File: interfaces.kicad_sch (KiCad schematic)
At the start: 92 parts, among them IC3 TPD8S009DSMR, J6 685119134923, J7 693071020811, J9 USB4105-GF-A, Q1 BSS138APW, Q10 BSS138APW, Q2 BSS138APW, Q3 BSS138APW, Q4 BSS138APW, Q5 BSS138APW, Q6 BSS138APW, Q9 BSS138APW, U7 FT4232HQ, Y2 ABM8G-12.000MHZ-18-D2Y-T

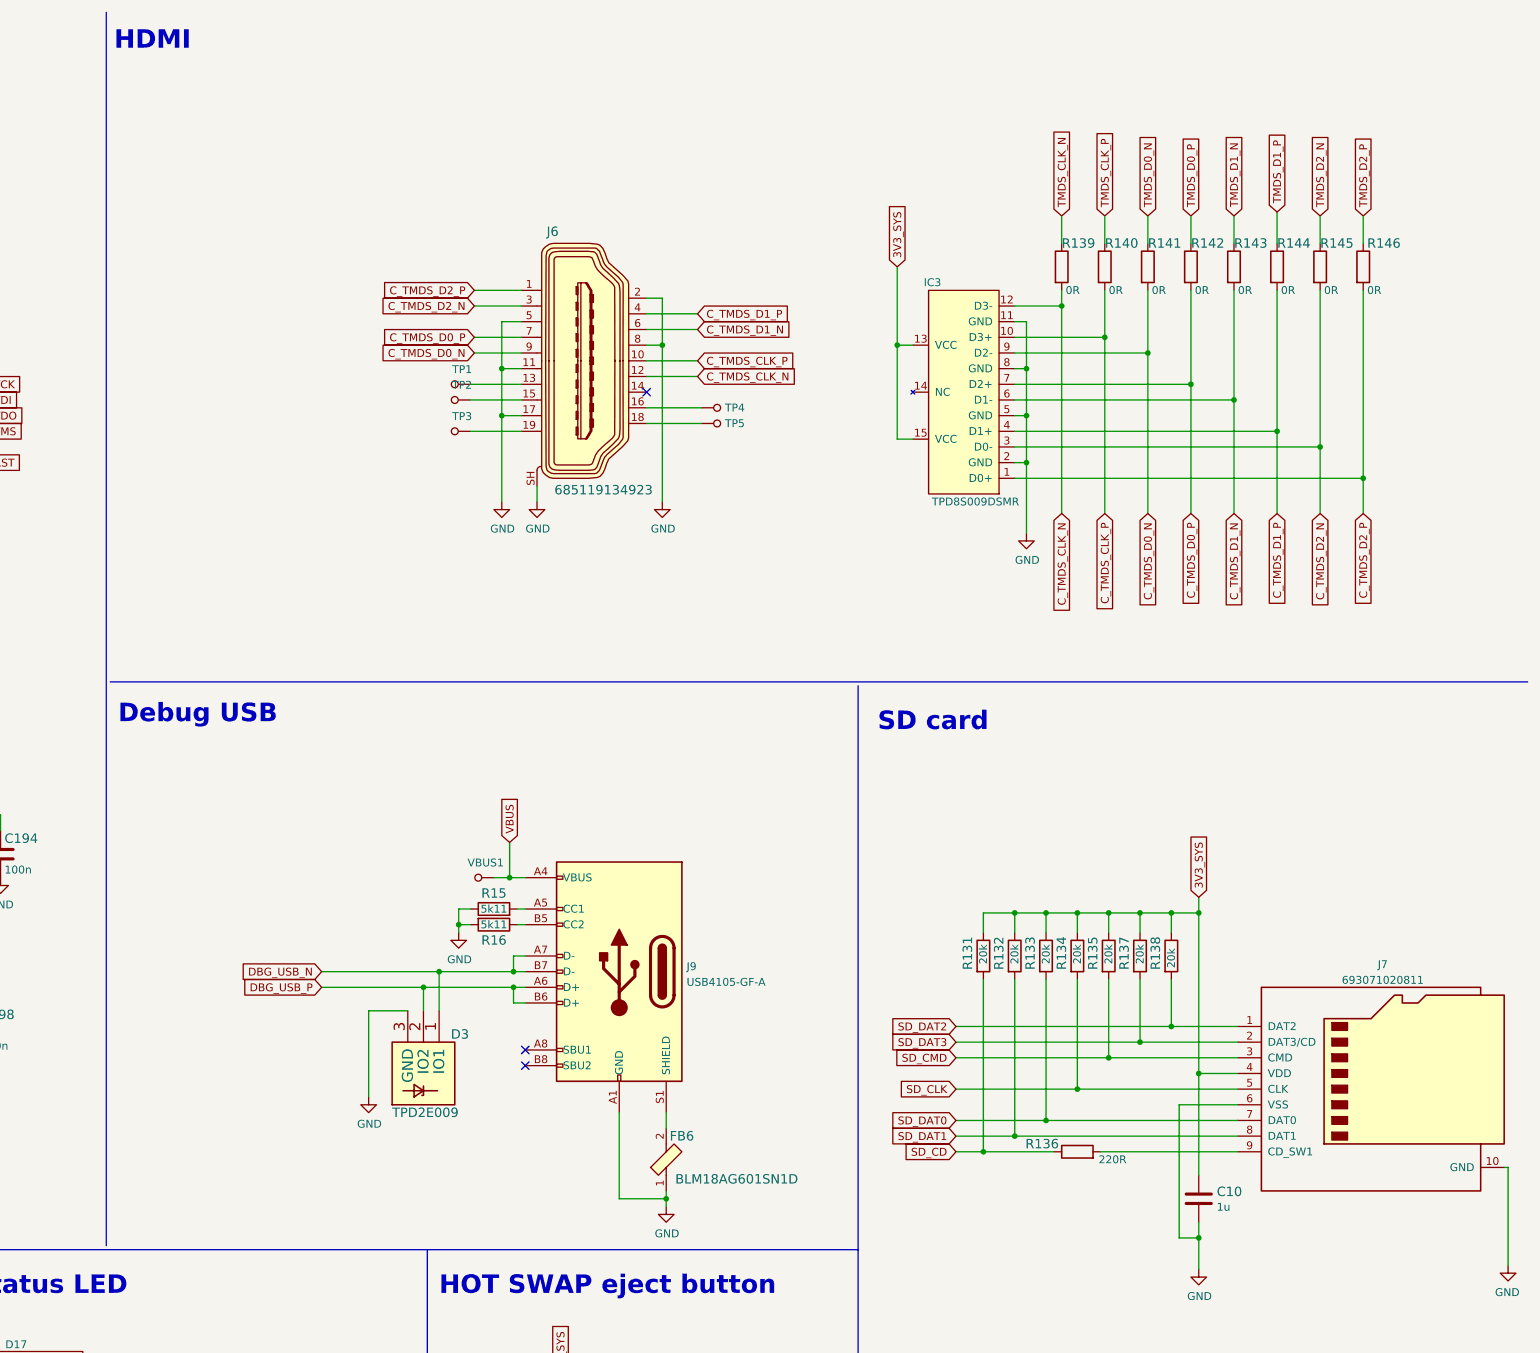
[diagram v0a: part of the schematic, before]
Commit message: Finish power supply polygons, improve connector shield to ground connection
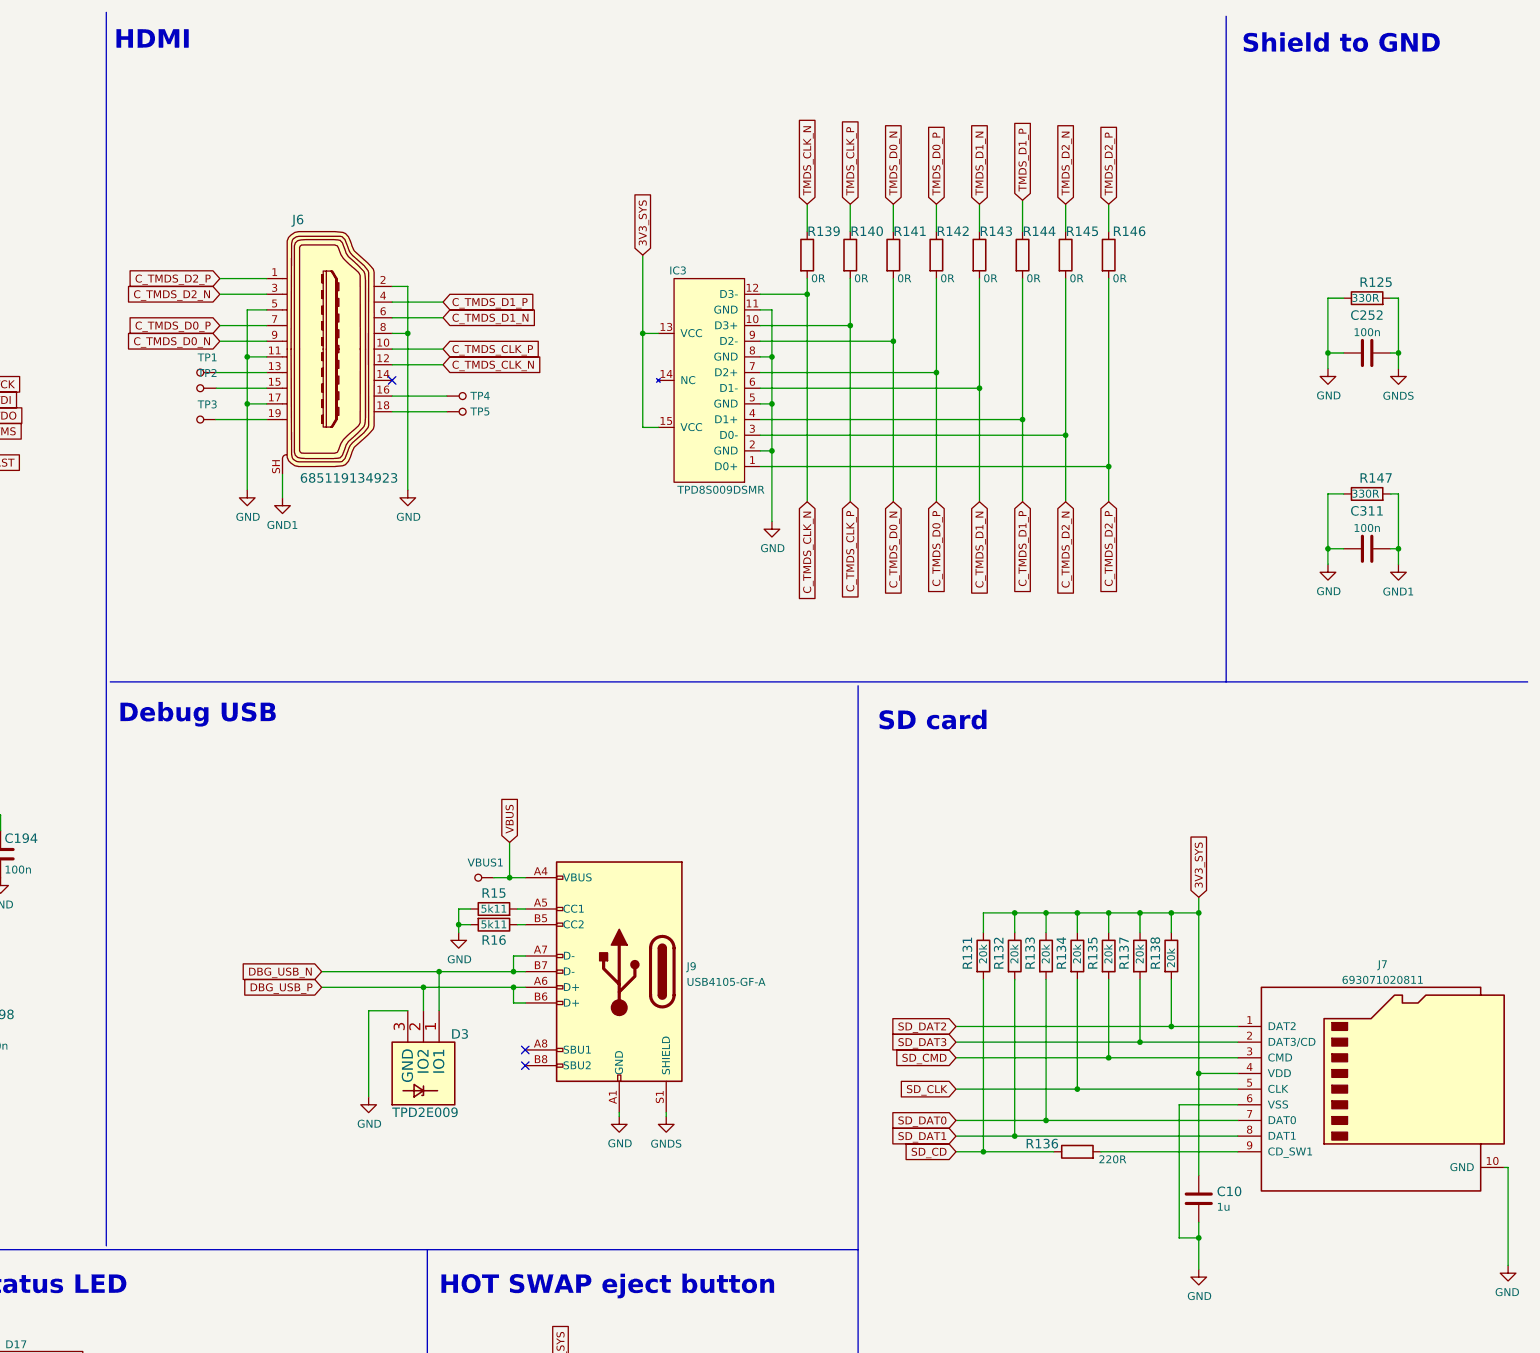
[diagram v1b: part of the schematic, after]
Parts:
- removed FB6: BLM18AG601SN1D, data-center-dram-tester-footprints:0603, symbol data-center-dram-tester:BLM18AG601SN1D
- added C252, C311: C_100n_0402, antmicro-footprints:0402-cap, symbol antmicroCapacitors0402:C_100n_0402
- added R125, R147: R_330R_0402, data-center-dram-tester-footprints:0402-res, symbol data-center-dram-tester:R_330R_0402
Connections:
- net GND: now also C252.1, C311.1, R125.1, R147.1; no longer J6.SH
- net GNDS: now reaches J9.S1 (SHIELD)
- net GNDS: now also C252.2, R125.2
- new net GND1: C311.2, J6.SH, R147.2
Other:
- note added: "Shield to GND"
- moved on the sheet: IC3, J6, R139, R140, R141, R142, R143, R144, R145, R146, TP1, TP2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

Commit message: Readability improvements
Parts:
- Y2: VAL (none) -> 12MHz
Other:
- moved on the sheet: C226, IC3, R125, R129, R130, R139, R140, R141, R142, R144, R145, R146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

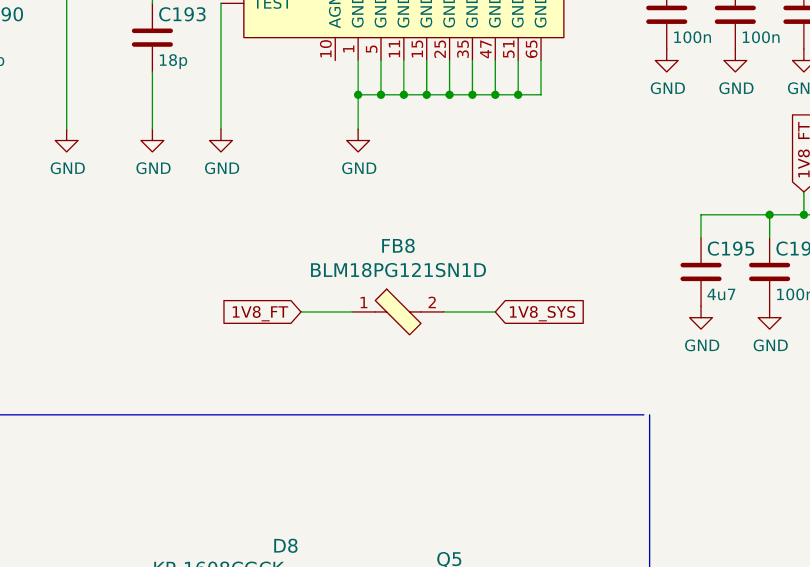
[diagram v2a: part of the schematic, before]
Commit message: Progress in HS matching and deskewing, clear DRC, implement schematic review changes, SI improvments
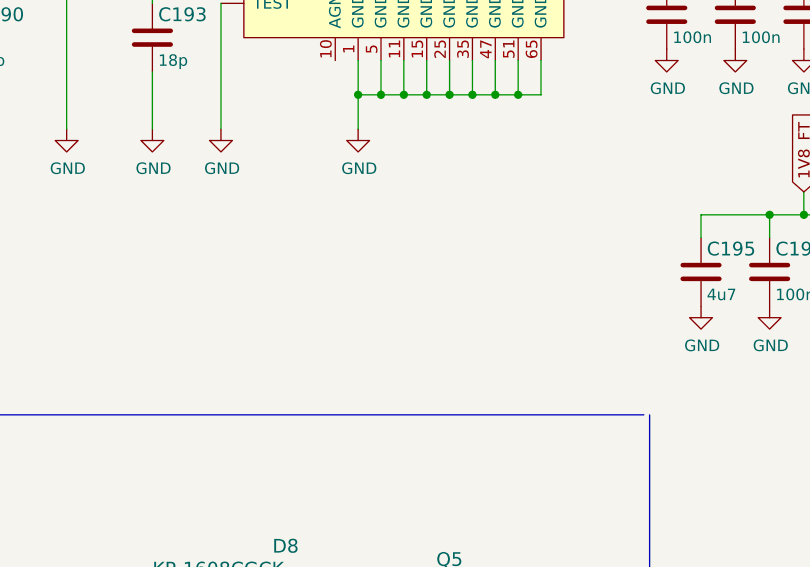
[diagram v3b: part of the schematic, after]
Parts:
- removed FB8: BLM18PG121SN1D, data-center-dram-tester-footprints:0603-res, symbol data-center-dram-tester:BLM18PG121SN1D
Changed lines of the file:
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@@
     (stroke (width 0) (type default) (color 0 0 0 0))
   )
-  (wire (pts (xy 105.41 181.61) (xy 111.125 181.61))
-    (stroke (width 0) (type default) (color 0 0 0 0))
-  )
   (wire (pts (xy 257.175 261.62) (xy 257.175 265.43))
     (stroke (width 0) (type default) (color 0 0 0 0))
@@
     (stroke (width 0) (type default) (color 0 0 0 0))
   )
-  (wire (pts (xy 89.535 181.61) (xy 95.25 181.61))
-    (stroke (width 0) (type default) (color 0 0 0 0))
-  )
   (wire (pts (xy 220.345 173.99) (xy 220.345 187.96))
     (stroke (width 0) (type default) (color 0 0 0 0))
@@
     )
   )
-  (global_label "1V8_FT" (shape input) (at 89.535 181.61 180) (fields_autoplaced)
-    (effects (font (size 1.27 1.27)) (justify right))
-    (property "Intersheet References" "${INTERSHEET_REFS}" (id 0) (at 0 0 0)
-      (effects (font (size 1.27 1.27)) hide)
-    )
-  )
   (global_label "HOT_SWAP_BUTTON" (shape input) (at 274.955 245.11 0) (fields_autoplaced)
     (effects (font (size 1.27 1.27)) (justify left))
@@
     )
   )
-  (global_label "1V8_SYS" (shape input) (at 111.125 181.61 0) (fields_autoplaced)
-    (effects (font (size 1.27 1.27)) (justify left))
-    (property "Intersheet References" "${INTERSHEET_REFS}" (id 0) (at 0 0 0)
-      (effects (font (size 1.27 1.27)) hide)
-    )
-  )
   (global_label "UART1_TX" (shape input) (at 148.59 118.11 0) (fields_autoplaced)
     (effects (font (size 1.27 1.27)) (justify left))
@@
     )
     (pin "1")
-    (pin "2")
-  )
-  (symbol (lib_id "data-center-dram-tester:BLM18PG121SN1D") (at 100.33 181.61 0) (unit 1)
-    (in_bom yes) (on_board yes)
-    (property "Reference" "FB8" (id 0) (at 100.33 174.3202 0)
-      (effects (font (size 1.524 1.524)))
-    )
-    (property "Value" "BLM18PG121SN1D" (id 1) (at 100.33 177.0126 0)
-      (effects (font (size 1.524 1.524)))
-    )
-    (property "Footprint" "data-center-dram-tester-footprints:0603-res" (id 2) (at 105.41 176.53 0)
-      (effects (font (size 1.524 1.524)) (justify left) hide)
-    )
-    (property "Datasheet" "https://www.murata.com/en-us/products/productdata/8796738650142/ENFA0003.pdf" (id 3) (at 105.41 173.99 0)
-      (effects (font (size 1.524 1.524)) (justify left) hide)
-    )
-    (property "MPN" "BLM18PG121SN1D" (id 4) (at 105.41 168.91 0)
-      (effects (font (size 1.524 1.524)) (justify left) hide)
-    )
-    (property "Manufacturer" "Murata Electronics North America" (id 5) (at 105.41 153.67 0)
-      (effects (font (size 1.524 1.524)) (justify left) hide)
-    )
-    (pin "1")

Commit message: Add remarks after review to the schenatic
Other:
- note added: "TODO: Replace FT4232HQ with FT4232H-56Q"
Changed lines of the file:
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@@
     )
+  )
+  (text "TODO: Replace FT4232HQ with FT4232H-56Q" (at 424.18 82.55 0)
+    (effects (font (size 1.27 1.27)) (justify left bottom))
   )
   (text "User LEDs" (at 16.51 200.66 0)

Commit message: DDR SI improvments, optimize bom, apply review issues fix
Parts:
- removed C194, C198: C_100n_0402_6V3, data-center-dram-tester-footprints:0402-cap, symbol data-center-dram-tester:C_100n_0402_6V3
- removed U7: FT4232HQ, data-center-dram-tester-footprints:FT4232HQ, symbol data-center-dram-tester:FT4232HQ
- added U7: FT4232H-56Q, antmicro-footprints:QFN-56-1EP_8x8mm_P0.5mm_EP5.5.9x5.9mm, symbol antmicroInterfaceControllers:FT4232H-56Q
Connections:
- net 1V8_FT: now also U7.2 (VCORE), U7.31 (VCORE), U7.43 (VREGOUT)
- net 3V3_SYS: now also U7.16 (VCCIO), U7.36 (VCCIO), U7.44 (VREGIN), U7.50 (VCCIO)
- net DBG_USB_N: now also U7.7 (DM)
- net DBG_USB_P: now also U7.8 (DP)
- net GND: now also U7.10 (TEST), U7.21 (GND), U7.41 (GND), U7.45 (GND), U7.57 (GND)
- net at R1.1: now also U7.22 (BDBUS0)
- net at R2.1: now also U7.23 (BDBUS1)
- net at R3.1: now also U7.24 (BDBUS2)
- net at R4.1: now also U7.25 (BDBUS3)
- net at R6.1: now also U7.32 (CDBUS0)
- net at R37.1: now also U7.46 (DDBUS1)
- net at R7.1: now also U7.33 (CDBUS1)
- net at R8.1: now also U7.42 (DDBUS0)
- net at C185.1, C189.1, FB5.2: now also U7.5 (VPHY)
- net at C184.1, C187.1, FB4.2: now also U7.9 (VPLL)
- net at R129.2: now also U7.6 (REF)
- net at R130.2: now also U7.11 (RESET)
- net at C190.1, Y2.1: now also U7.3 (OSCI)
- net at C193.1, Y2.3: now also U7.4 (OSCO)
- net at R18.1: now also U7.12 (ADBUS0)
- net at R19.1: now also U7.13 (ADBUS1)
- net at R20.1: now also U7.14 (ADBUS2)
- net at R25.1: now also U7.15 (ADBUS3)
- net at TP11.1: now also U7.18 (ADBUS5)
- net at R5.1: now also U7.27 (BDBUS5)
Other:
- note removed: "TODO: Replace FT4232HQ with FT4232H-56Q"

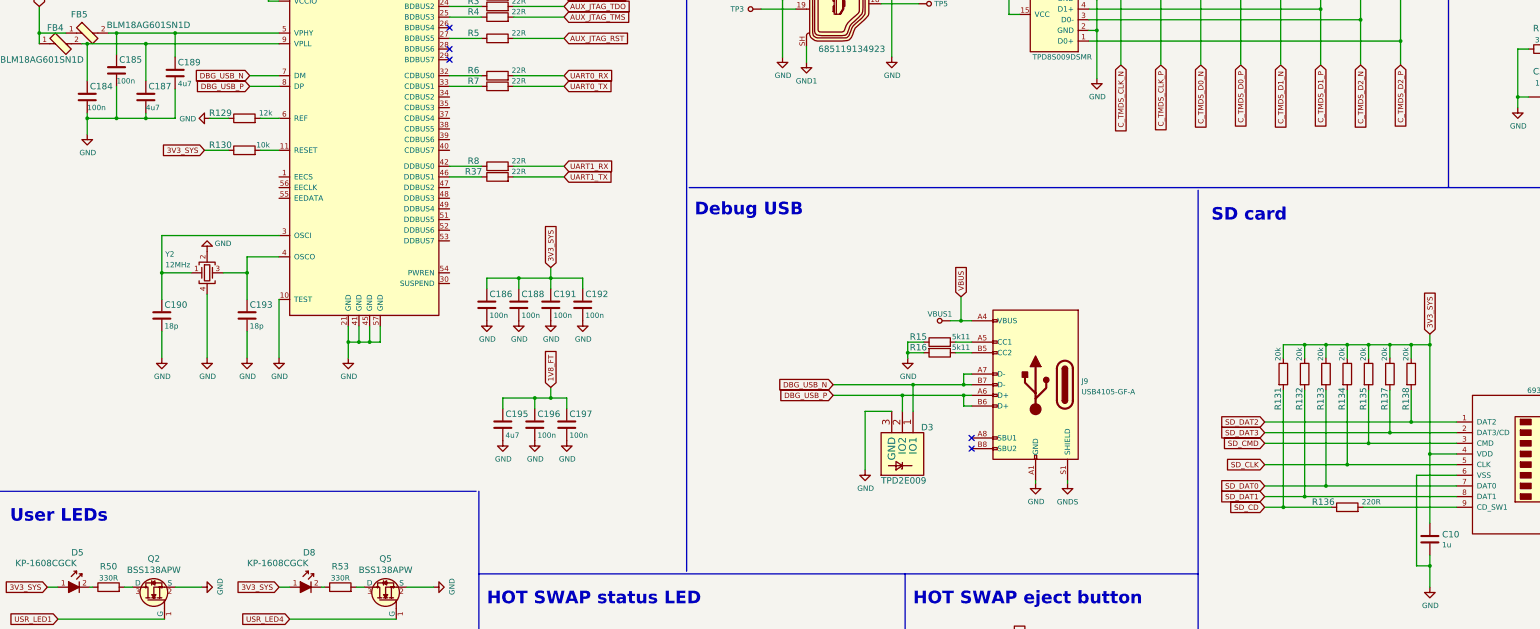
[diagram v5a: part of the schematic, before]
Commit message: Implement all review fixes, route control signals from FMC to FPGA
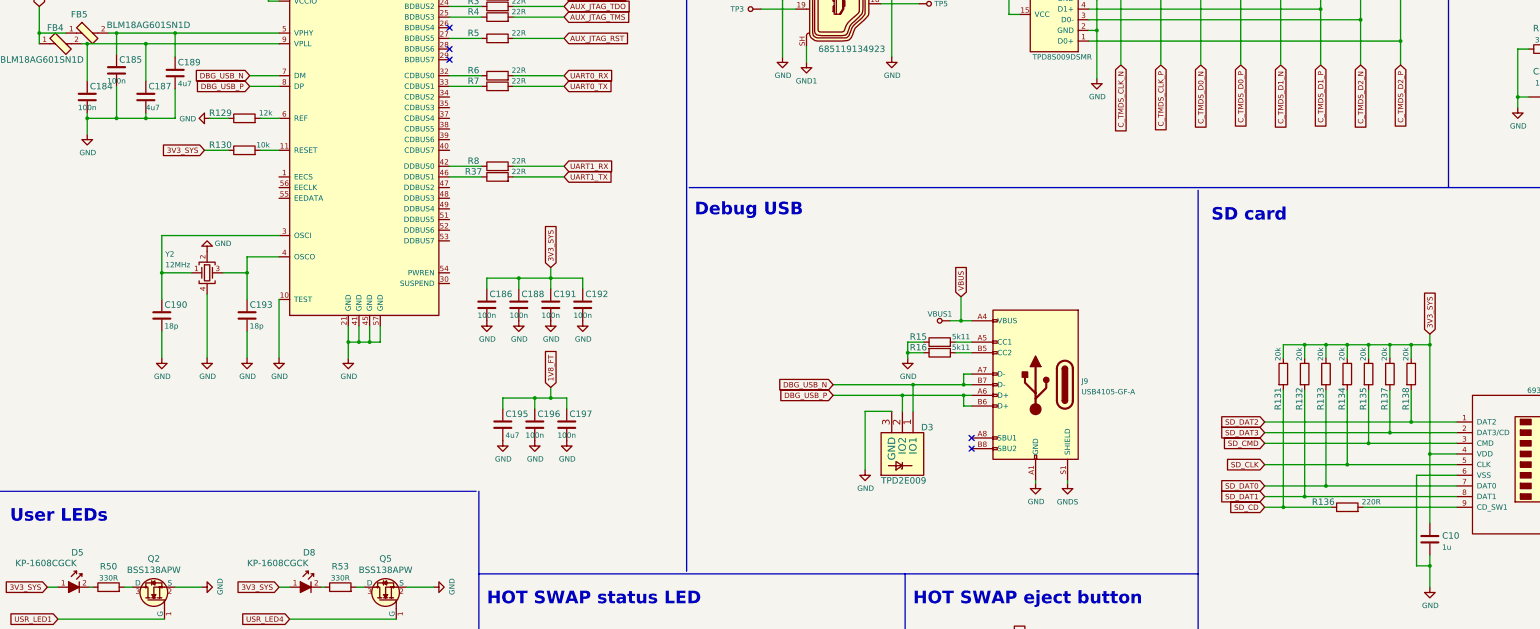
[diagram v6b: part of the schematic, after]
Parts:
- removed C10: C_1u_0603, data-center-dram-tester-footprints:0603-cap, symbol data-center-dram-tester:C_1u_0603
- added C10: C_1u_0402, antmicro-footprints:0402-cap, symbol antmicroCapacitors0402:C_1u_0402
- C184, C185, C186, C188, C191, C192, C196, C197: value C_100n_0402_6V3 -> C_100n_0402; footprint data-center-dram-tester-footprints:0402-cap -> antmicro-footprints:0402-cap; symbol data-center-dram-tester:C_100n_0402_6V3 -> antmicroCapacitors0402:C_100n_0402; MPN 0402X104K6R3CT -> GRM155R61H104KE14D; Manufacturer Walsin -> Murata
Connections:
- net 3V3_SYS: now also C10.1
- net GND: now also C10.2
